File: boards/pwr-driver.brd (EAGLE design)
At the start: 99 x 56 mm, 24 parts

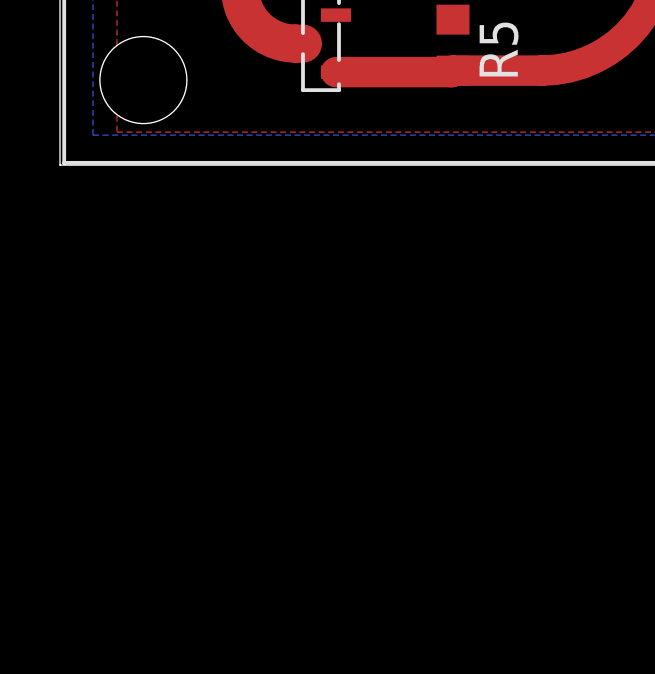
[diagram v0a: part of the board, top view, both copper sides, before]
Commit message: dding start of parts lib for breakout board.
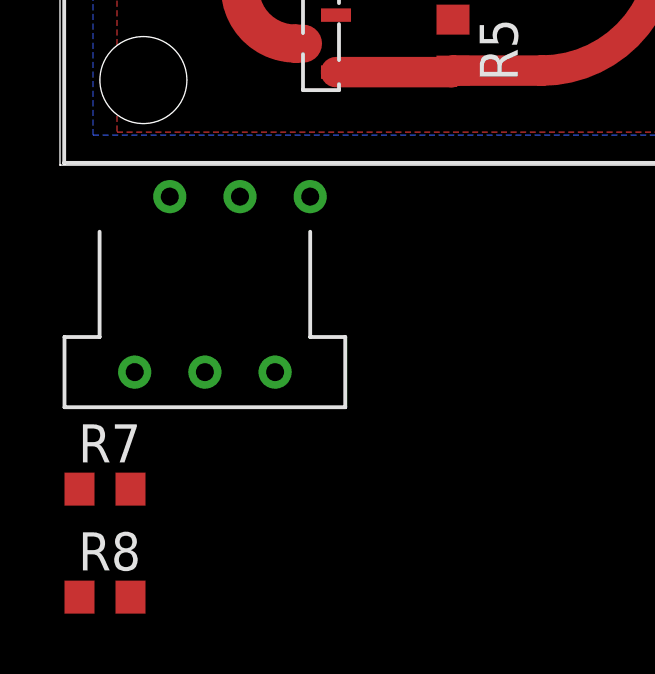
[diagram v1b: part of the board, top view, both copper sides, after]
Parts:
- added R7, R8: (no value), resistor:R0603
- added U$1: MPM80, needed-parts:TO-220-8L
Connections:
- new net BATT: R7.2
- new net N$15: U$1.P$6
- new net N$4: R7.1, R8.2, U$1.P$7
- net GND: now also R8.1, U$1.P$4, U$1.P$5
- net VIN: now also U$1.P$3
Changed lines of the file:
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@@
 <element name="R6" library="resistor" package="R0603" value="10k" x="87.8" y="5.9" rot="R180"/>
 <element name="C5" library="resistor" package="C0603" value=".1uf" x="87.8" y="3.1" rot="R180"/>
+<element name="U$1" library="needed-parts" package="TO-220-8L" value="MPM80" x="6" y="-6.9"/>
+<element name="R7" library="resistor" package="R0603" value="" x="1.5" y="-10.8"/>
+<element name="R8" library="resistor" package="R0603" value="" x="1.5" y="-14.4"/>
 </elements>
 <signals>
@@
 <via x="67.6" y="9.6" extent="1-16" drill="0.6"/>
 <via x="72.7" y="9.6" extent="1-16" drill="0.6"/>
-<wire x1="59.825" y1="41" x2="59.825" y2="37.675" width="0" layer="19" extent="16-16"/>
+<contactref element="R8" pad="1"/>
+<contactref element="U$1" pad="P$4"/>
+<contactref element="U$1" pad="P$5"/>
+<wire x1="71.4" y1="48.3" x2="91.4" y2="44.1" width="0" layer="19" extent="1-1"/>
+<wire x1="64.3" y1="52.1" x2="71.4" y2="48.3" width="0" layer="19" extent="1-1"/>
+<wire x1="60.4" y1="53.1" x2="64.3" y2="52.1" width="0" layer="19" extent="1-16"/>
+<wire x1="62.6" y1="44.9" x2="60.8" y2="48.4" width="0" layer="19" extent="1-16"/>
+<wire x1="59.825" y1="41" x2="62.6" y2="44.9" width="0" layer="19" extent="1-16"/>
+<wire x1="59.825" y1="37.675" x2="59.825" y2="41" width="0" layer="19" extent="16-16"/>
+<wire x1="60.89" y1="34.24" x2="61.9" y2="35.6" width="0" layer="19" extent="16-16"/>
+<wire x1="60.89" y1="29.94" x2="60.89" y2="34.24" width="0" layer="19" extent="16-16"/>
+<wire x1="61.5" y1="25.6" x2="60.89" y2="29.94" width="0" layer="19" extent="16-16"/>
+<wire x1="61.9" y1="23.7" x2="61.5" y2="25.6" width="0" layer="19" extent="16-16"/>
+<wire x1="53.8" y1="36.15" x2="59.825" y2="37.675" width="0" layer="19" extent="16-16"/>
+<wire x1="73.4" y1="18.9" x2="67" y2="17.3" width="0" layer="19" extent="1-1"/>
+<wire x1="74.4" y1="21.25" x2="73.4" y2="18.9" width="0" layer="19" extent="1-1"/>
+<wire x1="76.6" y1="21.25" x2="74.4" y2="21.25" width="0" layer="19" extent="1-1"/>
+<wire x1="76.6" y1="27.7" x2="76.6" y2="21.25" width="0" layer="19" extent="1-1"/>
+<wire x1="74.6" y1="29.4" x2="76.6" y2="27.7" width="0" layer="19" extent="1-1"/>
+<wire x1="67.64" y1="30.4" x2="60.89" y2="29.94" width="0" layer="19" extent="16-16"/>
+<wire x1="67.6" y1="9.6" x2="67" y2="17.3" width="0" layer="19" extent="1-1"/>
+<wire x1="72.7" y1="9.6" x2="67.6" y2="9.6" width="0" layer="19" extent="1-1"/>
+<wire x1="42.6" y1="49.45" x2="51.5162" y2="52.605" width="0" layer="19" extent="1-1"/>
+<wire x1="43" y1="46.7" x2="42.6" y2="49.45" width="0" layer="19" extent="1-1"/>
+<wire x1="38.8" y1="50.3" x2="42.6" y2="49.45" width="0" layer="19" extent="1-1"/>
+<wire x1="33.02" y1="50.8" x2="38.8" y2="50.3" width="0" layer="19" extent="1-1"/>
+<wire x1="25.4" y1="53.34" x2="33.02" y2="50.8" width="0" layer="19" extent="1-1"/>
+<wire x1="17.78" y1="53.34" x2="25.4" y2="53.34" width="0" layer="19" extent="1-1"/>
+<wire x1="83.86" y1="13.36" x2="76.6" y2="21.25" width="0" layer="19" extent="1-1"/>
+<wire x1="88.36" y1="13.36" x2="83.86" y2="13.36" width="0" layer="19" extent="1-1"/>
+<wire x1="83.86" y1="8.36" x2="83.86" y2="13.36" width="0" layer="19" extent="1-1"/>
+<wire x1="88.65" y1="5.9" x2="83.86" y2="8.36" width="0" layer="19" extent="1-1"/>
+<wire x1="88.65" y1="3.1" x2="88.65" y2="5.9" width="0" layer="19" extent="1-1"/>
+<wire x1="92.6" y1="4.1" x2="88.65" y2="3.1" width="0" layer="19" extent="1-1"/>
+<wire x1="92.3" y1="19.5" x2="88.36" y2="13.36" width="0" layer="19" extent="1-1"/>
+<wire x1="9.6" y1="34.4" x2="15.24" y2="45.72" width="0" layer="19" extent="1-1"/>
+<wire x1="3.1" y1="20.6" x2="9.6" y2="34.4" width="0" layer="19" extent="1-1"/>
+<wire x1="49.75" y1="7.4" x2="60.6" y2="19.6" width="0" layer="19" extent="16-16"/>
+<wire x1="35.5" y1="8.3" x2="49.75" y2="7.4" width="0" layer="19" extent="1-1"/>
+<wire x1="9.2" y1="5" x2="3.1" y2="20.6" width="0" layer="19" extent="1-1"/>
+<wire x1="13.1" y1="4.85" x2="9.2" y2="5" width="0" layer="19" extent="1-1"/>
+<wire x1="6" y1="-1.05" x2="9.2" y2="5" width="0" layer="19" extent="1-1"/>
+<wire x1="4.83" y1="-6.9" x2="6" y2="-1.05" width="0" layer="19" extent="1-1"/>
+<wire x1="0.65" y1="-14.4" x2="4.83" y2="-6.9" width="0" layer="19" extent="1-1"/>
+<wire x1="40.9" y1="24.3" x2="35.5" y2="8.3" width="0" layer="19" extent="1-1"/>
+<wire x1="25.7" y1="24.6" x2="40.9" y2="24.3" width="0" layer="19" extent="1-1"/>
 </signal>
 <signal name="3V3">
@@
 <wire x1="54.83" y1="9.23" x2="54.83" y2="7.4" width="1.4224" layer="1"/>
 <wire x1="68.6" y1="43.3" x2="68.6" y2="44.9" width="0.4064" layer="1"/>
+<contactref element="U$1" pad="P$3"/>
+<wire x1="7.17" y1="-6.9" x2="54.83" y2="7.4" width="0" layer="19" extent="1-1"/>
 </signal>
 <signal name="N$8">
@@
 <wire x1="10.16" y1="50.8" x2="86.95" y2="7.35" width="0" layer="19" extent="1-1"/>
 </signal>
+<signal name="N$4">
+<contactref element="R7" pad="1"/>
+<contactref element="R8" pad="2"/>
+<contactref element="U$1" pad="P$7"/>
+<wire x1="0.65" y1="-10.8" x2="2.35" y2="-14.4" width="0" layer="19" extent="1-1"/>
+<wire x1="2.49" y1="-6.9" x2="0.65" y2="-10.8" width="0" layer="19" extent="1-1"/>
+</signal>
+<signal name="N$15">
+<contactref element="U$1" pad="P$6"/>
+</signal>
+<signal name="BATT">
+<contactref element="R7" pad="2"/>
+</signal>
 </signals>

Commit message: Added more parts and a readme.
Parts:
- removed IC1: (no value), v-reg:78XXS
- removed JP1: (no value), pinhead:1X06
- removed R5: 10k, resistor:R0603
- removed U$10: NPN-T-SMALL, mgregg:SOT23
- removed U$7: OKR-T-W12-DC-TO-DC, mgregg:OKR-T-W12
- added BATT: (no value), pinhead:1X02
- added U$3: STEP-UP-FROM-AMAZON, needed-parts:STEP-UP-FROM-AMAZON
- moved R8 76.7 mm to (70.0, 20.0), turned to 180 degrees
- moved U$1 73.8 mm to (71.8, 26.6), turned to 90 degrees
- moved R7 71.6 mm to (66.1, 20.0), turned to 180 degrees
- moved C4 9.44 mm to (62.3, 10.1)
- moved R1 5.84 mm to (73.7, 16.3)
- moved R2 5.61 mm to (76.9, 16.5)
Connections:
- removed net N$15: U$1.P$6
- removed net N$8: U$7.REMOTE
- removed net SCREEN1: U$10.P$3
- net 3V3: no longer JP1.2
- net 5V: now also U$3.OUT+; no longer IC1.OUT, U$7.VOUT
- net BATT: now also BATT.1, U$1.P$6, U$3.IN+
- net GND: now also BATT.2, U$3.GND, U$3.IN-, U$3.OUT-; no longer IC1.GND, JP1.1, R5.1, U$10.P$2, U$7.GND
- net GPIO25: no longer JP1.4
- net SCL: no longer JP1.6
- net SCREEN: no longer R5.2, U$10.P$1
- net SDA: no longer JP1.5
- net TRIM: no longer U$7.TRIM
- net VIN: no longer IC1.IN, JP1.3, U$7.VIN
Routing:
- net 5V: track 123.8 -> 2.54 mm, vias 1 -> 0
- net GPIO25: track 96.1 -> 0.00 mm
- net BATT: track 0.00 -> 66.6 mm
- net VIN: track 75.9 -> 18.5 mm
- net SCL: track 55.6 -> 8.70 mm
- net SDA: track 46.8 -> 8.13 mm
- net SCREEN: track 12.6 -> 0.00 mm
- net GND: track 56.0 -> 44.0 mm, vias 17 -> 7
- net N$4: track 0.00 -> 6.67 mm
- net TRIM: track 5.33 -> 0.00 mm
- net SCREEN1: track 5.19 -> 0.00 mm
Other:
- board text added: "4 to 5 v converter"
- board text removed: "270"
- board text removed: "43k"
- board text removed: "7805"
- board text removed: "C4"
- board text removed: "CinchCircuits.com"
- board text removed: "DC-2-DC"
- board text removed: "ISP"
- board text removed: "In"
- board text removed: "Max Input Voltage Dependant on C-IN."
- board text removed: "Pan"
- board text removed: "Pan-tilt-Pi"
- board text removed: "R1"
- board text removed: "R2"
- board text removed: "Tilt"

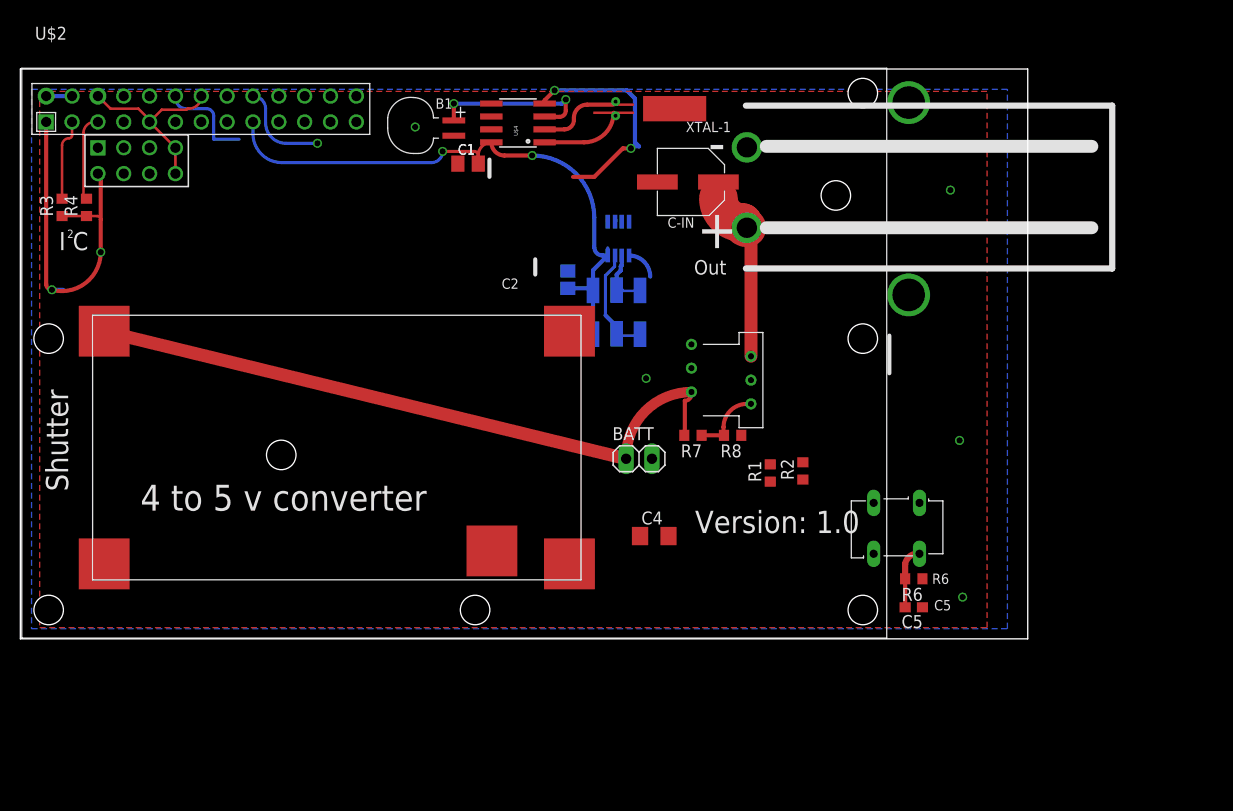
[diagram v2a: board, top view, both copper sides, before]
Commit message: Converted to three pin powerpole.
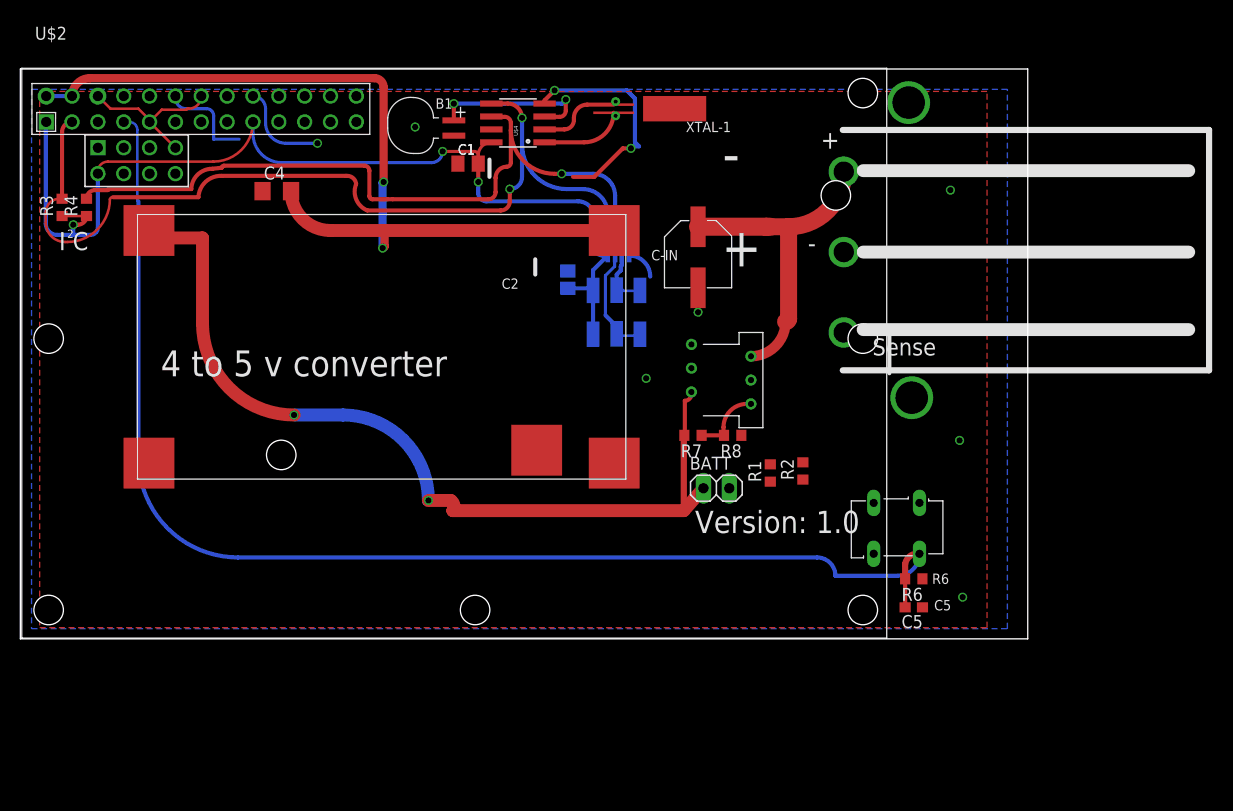
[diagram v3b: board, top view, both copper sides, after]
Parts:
- removed U$8: ANDERSON-DUAL, mgregg:POWERPOLE-DUAL
- added U$7: POWERPOLE-WITH-SENSE, needed-parts:POWERPOLE-3
- moved C4 50.3 mm to (25.2, 44.0)
- moved U$3 10.8 mm to (35.5, 28.7)
- moved U$11 10.2 mm to (69.9, 34.5), turned to 90 degrees
- moved BATT 8.13 mm to (68.4, 14.8)
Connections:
- new net IGNITION: U$7.SENSE
- net GND: now also U$7.NEG; no longer U$8.NEG
- net VIN: now also U$7.POS; no longer U$8.POS
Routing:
- net GPIO4: track 5.98 -> 122.4 mm
- net 5V: track 2.54 -> 85.3 mm, vias 0 -> 2
- net SDA: track 8.13 -> 87.2 mm, vias 0 -> 2
- net SCL: track 8.70 -> 69.7 mm, vias 0 -> 1
- net BATT: track 66.6 -> 84.2 mm, vias 0 -> 2
- net VIN: track 18.5 -> 31.2 mm
- net 3V3: track 93.8 -> 102.9 mm, vias 4 -> 3
- net GND: track 44.0 -> 41.4 mm, vias 7 -> 8
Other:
- board text removed: "Out"
- board text removed: "Shutter"

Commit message: Adding Version 1.0 boards with the submitted gerbers.
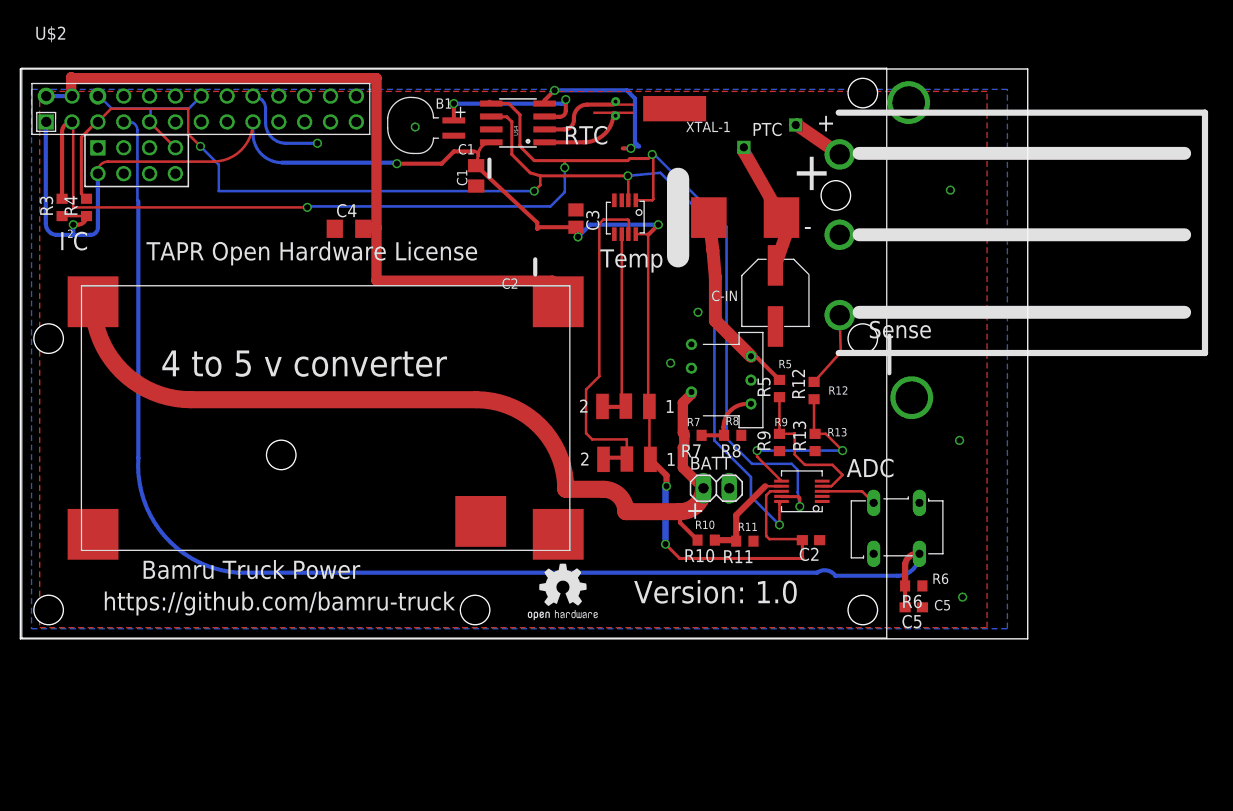
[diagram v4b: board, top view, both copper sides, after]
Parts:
- removed R1: 270, resistor:R0603
- removed R2: 43k, resistor:R0603
- added C2: .1uf, resistor:C0603
- added R10, R11, R12, R13, R5, R9: (no value), resistor:R0603
- added U$10: ADS1013, needed-parts:MSOP-10
- added U$15: DIODE-403, needed-parts:403
- added U$16: (no value), NBitWonder:OSHW2
- added U$8: PTC, needed-parts:PTC-0ZRM0100FF1E
- moved U$12 12.4 mm to (58.5, 18.1), flipped to the top
- moved U$13 11.5 mm to (58.4, 23.3), flipped to the top
- moved U$3 8.90 mm to (30.0, 21.7)
- moved U$11 8.50 mm to (77.5, 30.7)
- moved C4 8.01 mm to (32.3, 40.3)
- moved C3 6.05 mm to (54.6, 41.3), flipped to the top
- moved U$9 2.10 mm to (59.1, 43.1), flipped to the top
- moved U$7 1.75 mm to (80.8, 35.9)
- moved C1 1.44 mm to (44.8, 45.5), turned to 90 degrees
- moved R6 0.70 mm to (87.8, 5.20)
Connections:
- removed net TRIM: R1.2, R2.2
- removed net VIN: U$1.P$3, U$11.POS, U$7.POS
- new net ABATT: R10.1, R11.2, U$10.P$7
- new net AIGNITION: R12.1, R13.2, U$10.P$6
- new net AIN: R5.1, R9.2, U$10.P$4
- new net DIODE-OUT: R5.2, U$1.P$3, U$15.NEG
- new net N$17: U$10.P$5
- new net PTC-IN: U$7.POS, U$8.P$1
- new net PTC-OUT: U$11.POS, U$15.POS, U$8.P$2
- net 3V3: now also C2.2, U$10.P$8
- net BATT: now also R10.2
- net GND: now also C2.1, R11.1, R13.1, R9.1, U$10.P$3; no longer R1.1, R2.1
- net IGNITION: now also R12.2
- net SCL: now also U$10.P$10
- net SDA: now also U$10.P$9
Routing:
- net SCL: track 69.7 -> 125.6 mm, vias 1 -> 4
- net SDA: track 87.2 -> 140.9 mm, vias 2 -> 4
- net 3V3: track 102.9 -> 153.0 mm, vias 3 -> 6
- net VIN: track 31.2 -> 0.00 mm
- net N$7: track 8.55 -> 31.8 mm
- net AIGNITION: track 0.00 -> 19.2 mm, vias 0 -> 2
- net DIODE-OUT: track 0.00 -> 18.9 mm
- net AIN: track 0.00 -> 15.2 mm
- net PTC-OUT: track 0.00 -> 13.8 mm
- net N$9: track 3.61 -> 17.1 mm
- net ABATT: track 0.00 -> 10.3 mm
- net 5V: track 85.3 -> 75.1 mm, vias 2 -> 0
- net PWM: track 9.47 -> 0.00 mm
- net IGNITION: track 0.00 -> 7.56 mm
- net PTC-IN: track 0.00 -> 5.22 mm
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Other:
- board text added: "ADC"
- board text added: "Bamru Truck Power"
- board text added: "R10"
- board text added: "R11"
- board text added: "R12"
- board text added: "R13"
- board text added: "R5"
- board text added: "R7"
- board text added: "R8"
- board text added: "R9"
- board text added: "RTC"
- board text added: "TAPR Open Hardware License"
- board text added: "Temp"
- board text added: "https://github.com/bamru-truck"
- board text removed: "-"

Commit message: Added resistor values to all of the resistor dividors.
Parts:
- R10: value (none) -> 10k
- R11: value (none) -> 30000
- R12, R5: value (none) -> 20k
- R13, R9: value (none) -> 5.5k
- R7: value (none) -> 5250
- R8: value (none) -> 1000
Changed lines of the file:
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@@
 <element name="C5" library="resistor" package="C0603" value=".1uf" x="87.8" y="3.1" rot="R180"/>
 <element name="U$1" library="needed-parts" package="TO-220-8L" value="MPM80" x="71.8" y="26.6" rot="R90"/>
-<element name="R7" library="resistor" package="R0603" value="" x="66.1" y="20" rot="R180"/>
-<element name="R8" library="resistor" package="R0603" value="" x="70" y="20" rot="R180"/>
+<element name="R7" library="resistor" package="R0603" value="5250" x="66.1" y="20" rot="R180"/>
+<element name="R8" library="resistor" package="R0603" value="1000" x="70" y="20" rot="R180"/>
 <element name="U$3" library="needed-parts" package="STEP-UP-FROM-AMAZON" value="STEP-UP-FROM-AMAZON" x="30" y="21.7"/>
 <element name="BATT" library="pinhead" package="1X02" value="" x="68.4" y="14.8"/>
@@
 <element name="U$8" library="needed-parts" package="PTC-0ZRM0100FF1E" value="PTC" x="76.2" y="50.5" rot="R180"/>
 <element name="U$10" library="needed-parts" package="MSOP-10" value="ADS1013" x="76.8" y="13.5" rot="R90"/>
-<element name="R5" library="resistor" package="R0603" value="" x="74.6" y="24.6" rot="R90"/>
-<element name="R9" library="resistor" package="R0603" value="" x="74.6" y="19.3" rot="R90"/>
-<element name="R10" library="resistor" package="R0603" value="" x="67.4" y="9.7" rot="R180"/>
-<element name="R11" library="resistor" package="R0603" value="" x="71.2" y="9.6" rot="R180"/>
-<element name="R12" library="resistor" package="R0603" value="" x="78" y="24.4" rot="R90"/>
-<element name="R13" library="resistor" package="R0603" value="" x="78.1" y="19.3" rot="R90"/>
+<element name="R5" library="resistor" package="R0603" value="20k" x="74.6" y="24.6" rot="R90"/>
+<element name="R9" library="resistor" package="R0603" value="5.5k" x="74.6" y="19.3" rot="R90"/>
+<element name="R10" library="resistor" package="R0603" value="10k" x="67.4" y="9.7" rot="R180"/>
+<element name="R11" library="resistor" package="R0603" value="30000" x="71.2" y="9.6" rot="R180"/>
+<element name="R12" library="resistor" package="R0603" value="20k" x="78" y="24.4" rot="R90"/>
+<element name="R13" library="resistor" package="R0603" value="5.5k" x="78.1" y="19.3" rot="R90"/>
 <element name="C2" library="resistor" package="C0603" value=".1uf" x="77.7" y="9.7" rot="R180"/>
 <element name="U$15" library="needed-parts" package="403" value="DIODE-403" x="74.8" y="41.4"/>
